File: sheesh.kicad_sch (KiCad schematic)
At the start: 104 parts, among them J1 3305-0-15-80-47-27-10-0, J10 3305-0-15-80-47-27-10-0, J11 3305-0-15-80-47-27-10-0, J12 3305-0-15-80-47-27-10-0, J13 3305-0-15-80-47-27-10-0, J14 3305-0-15-80-47-27-10-0, J15 3305-0-15-80-47-27-10-0, J16 3305-0-15-80-47-27-10-0, J17 3305-0-15-80-47-27-10-0, J18 3305-0-15-80-47-27-10-0, J19 3305-0-15-80-47-27-10-0, J2 3305-0-15-80-47-27-10-0, J20 3305-0-15-80-47-27-10-0, J21 3305-0-15-80-47-27-10-0, J22 3305-0-15-80-47-27-10-0, J23 3305-0-15-80-47-27-10-0, J24 3305-0-15-80-47-27-10-0, J25 3305-0-15-80-47-27-10-0, J26 3305-0-15-80-47-27-10-0, J27 3305-0-15-80-47-27-10-0, J28 3305-0-15-80-47-27-10-0, J29 3305-0-15-80-47-27-10-0, J3 3305-0-15-80-47-27-10-0, J30 3305-0-15-80-47-27-10-0, J31 3305-0-15-80-47-27-10-0, J32 3305-0-15-80-47-27-10-0, J33 3305-0-15-80-47-27-10-0, J34 3305-0-15-80-47-27-10-0, J35 3305-0-15-80-47-27-10-0, J36 3305-0-15-80-47-27-10-0, J37 3305-0-15-80-47-27-10-0, J38 3305-0-15-80-47-27-10-0, J39 3305-0-15-80-47-27-10-0, J4 3305-0-15-80-47-27-10-0, J40 3305-0-15-80-47-27-10-0, J41 3305-0-15-80-47-27-10-0, J42 3305-0-15-80-47-27-10-0, J43 3305-0-15-80-47-27-10-0, J44 3305-0-15-80-47-27-10-0, J45 3305-0-15-80-47-27-10-0, J46 3305-0-15-80-47-27-10-0, J47 3305-0-15-80-47-27-10-0, J48 3305-0-15-80-47-27-10-0, J49 3305-0-15-80-47-27-10-0, J5 3305-0-15-80-47-27-10-0, J50 3305-0-15-80-47-27-10-0, J51 3305-0-15-80-47-27-10-0, J52 3305-0-15-80-47-27-10-0, J53 3305-0-15-80-47-27-10-0, J54 3305-0-15-80-47-27-10-0, J55 3305-0-15-80-47-27-10-0, J56 3305-0-15-80-47-27-10-0, J57 310-13-107-41-001000, J58 310-13-107-41-001000, J59 YZ00615050R-04, J6 3305-0-15-80-47-27-10-0, J60 YZ00615050R-04, J61 YZ00615050R-04, J62 YZ00615050R-04, J63 YZ00615050R-04, J64 310-13-107-41-001000, J65 310-13-107-41-001000, J66 YZ00615050R-04, J67 YZ00615050R-04, J68 YZ00615050R-04, J69 YZ00615050R-04, J7 3305-0-15-80-47-27-10-0, J70 YZ00615050R-04, J8 3305-0-15-80-47-27-10-0, J9 3305-0-15-80-47-27-10-0, SW1 SW_Push, SW10 SW_Push, SW11 SW_Push, SW12 SW_Push, SW13 SW_Push, SW14 SW_Push, SW15 SW_Push, SW16 SW_Push, SW17 SW_Push, SW18 SW_Push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

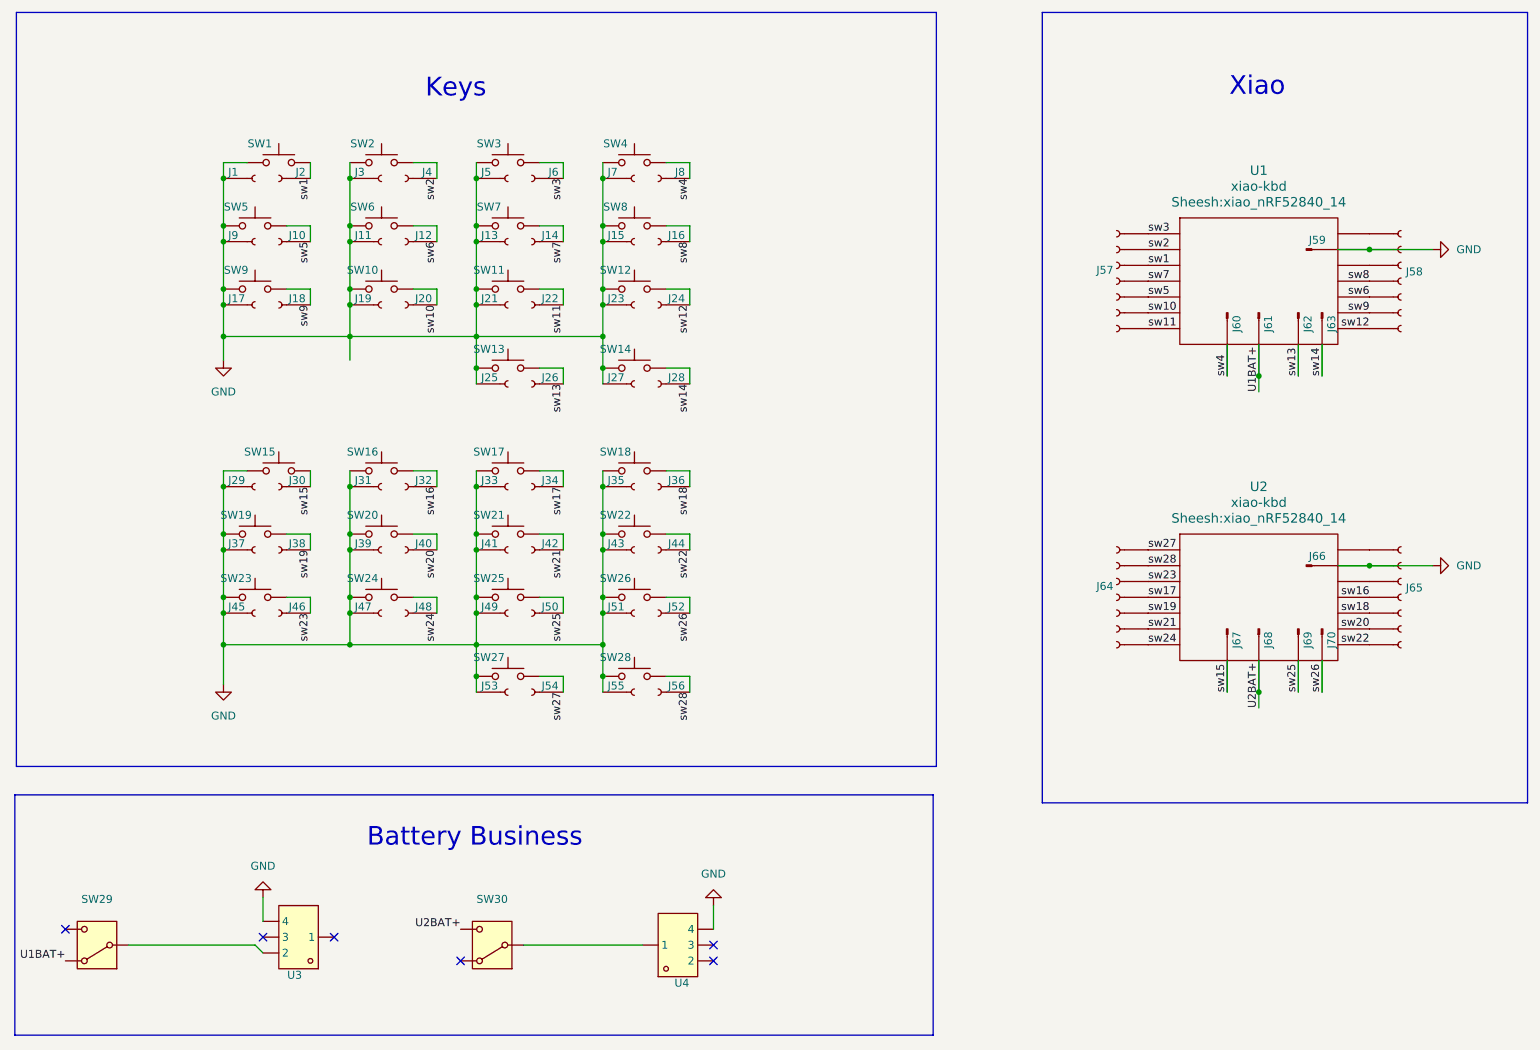
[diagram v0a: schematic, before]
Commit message: fix(sw-th_ssss811101): swap SW29 & SW30 symbol & footprint
Change PCM12SMTR to SSSS811101. The latter fits on the former's footprint, but the location was
slightly off fin  the cpl
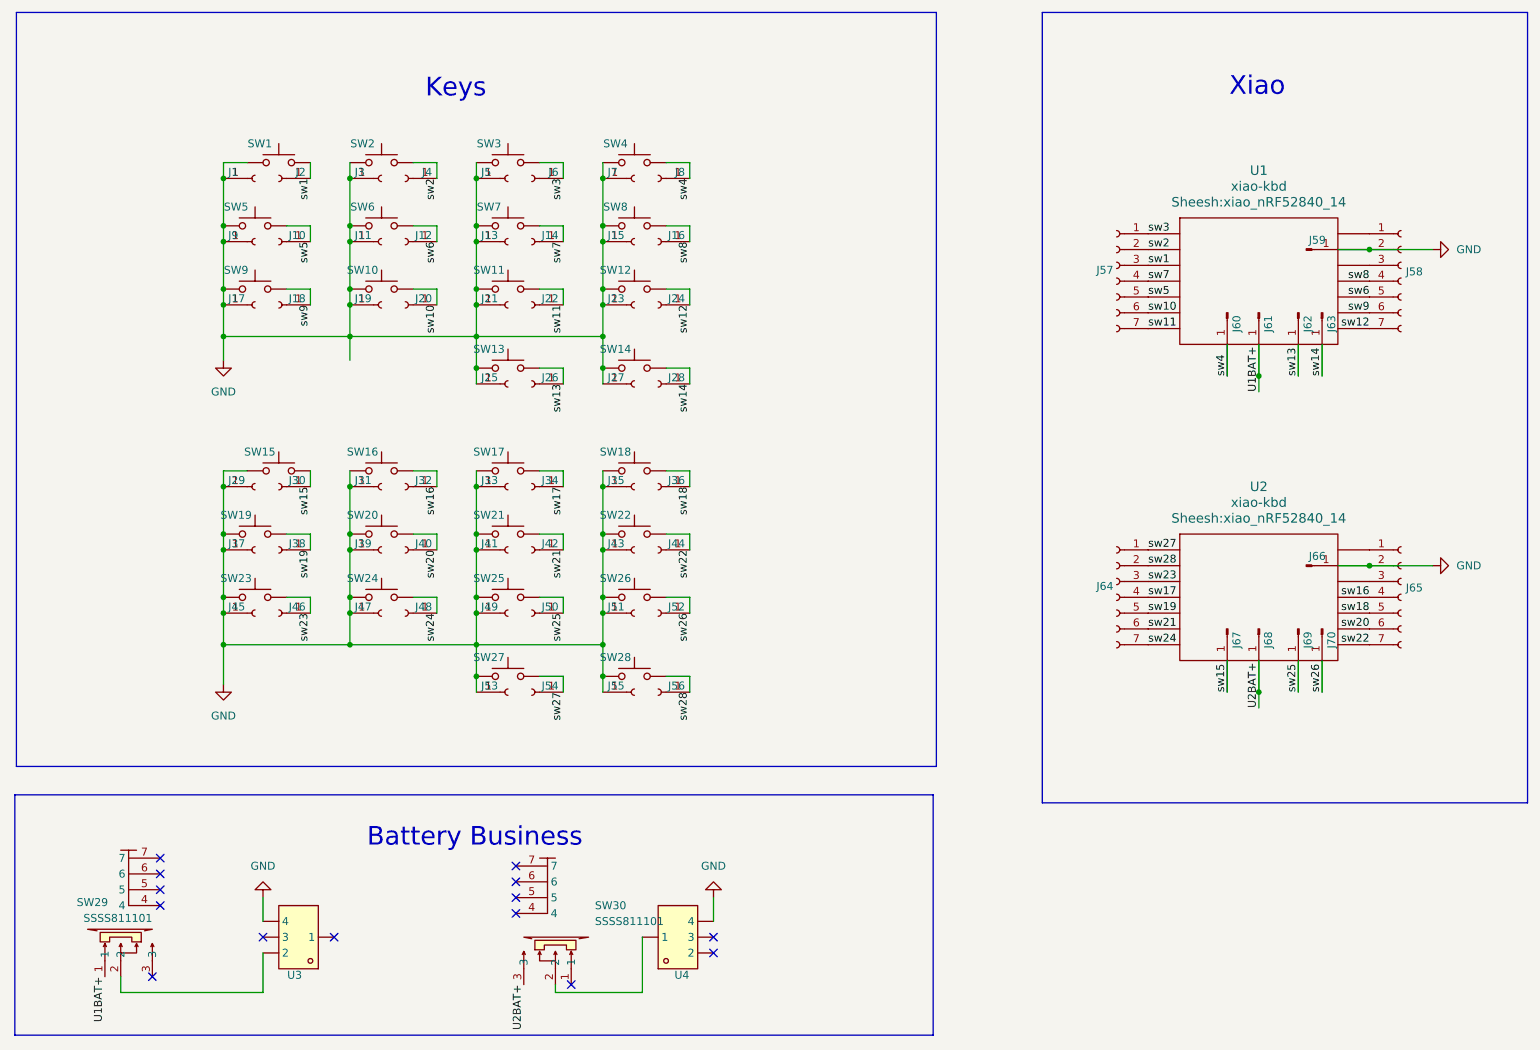
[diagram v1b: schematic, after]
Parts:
- removed SW29, SW30: SSSS811101, Sheesh:SW_PCM12SMTR, symbol Switch:SW_SPDT
- added SW29, SW30: SSSS811101, Sheesh:SW-SMD_SSSS811101, symbol Sheesh:SSSS811101
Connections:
- net U1BAT+: now also SW29.1
- net U2BAT+: now also SW30.3
- net at U4.1: now also SW30.2
- net at U3.2: now also SW29.2
- no-connect marks 6 -> 14
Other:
- moved on the sheet: U4

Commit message: fix(component): correct lcsc field name on ssss811101
correct lcsc field name so it passes kibot filter
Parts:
- SW29, SW30: LCSC (none) -> C109335; LCSC Part C109335 -> (none)
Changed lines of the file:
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@@
 			)
 		)
-		(property "LCSC Part" "C109335"
+		(property "LCSC" "C109335"
 			(at 40.64 151.13 0)
 			(effects
@@
 			)
 		)
-		(property "LCSC Part" "C109335"
+		(property "LCSC" "C109335"
 			(at 113.03 152.4 0)
 			(effects

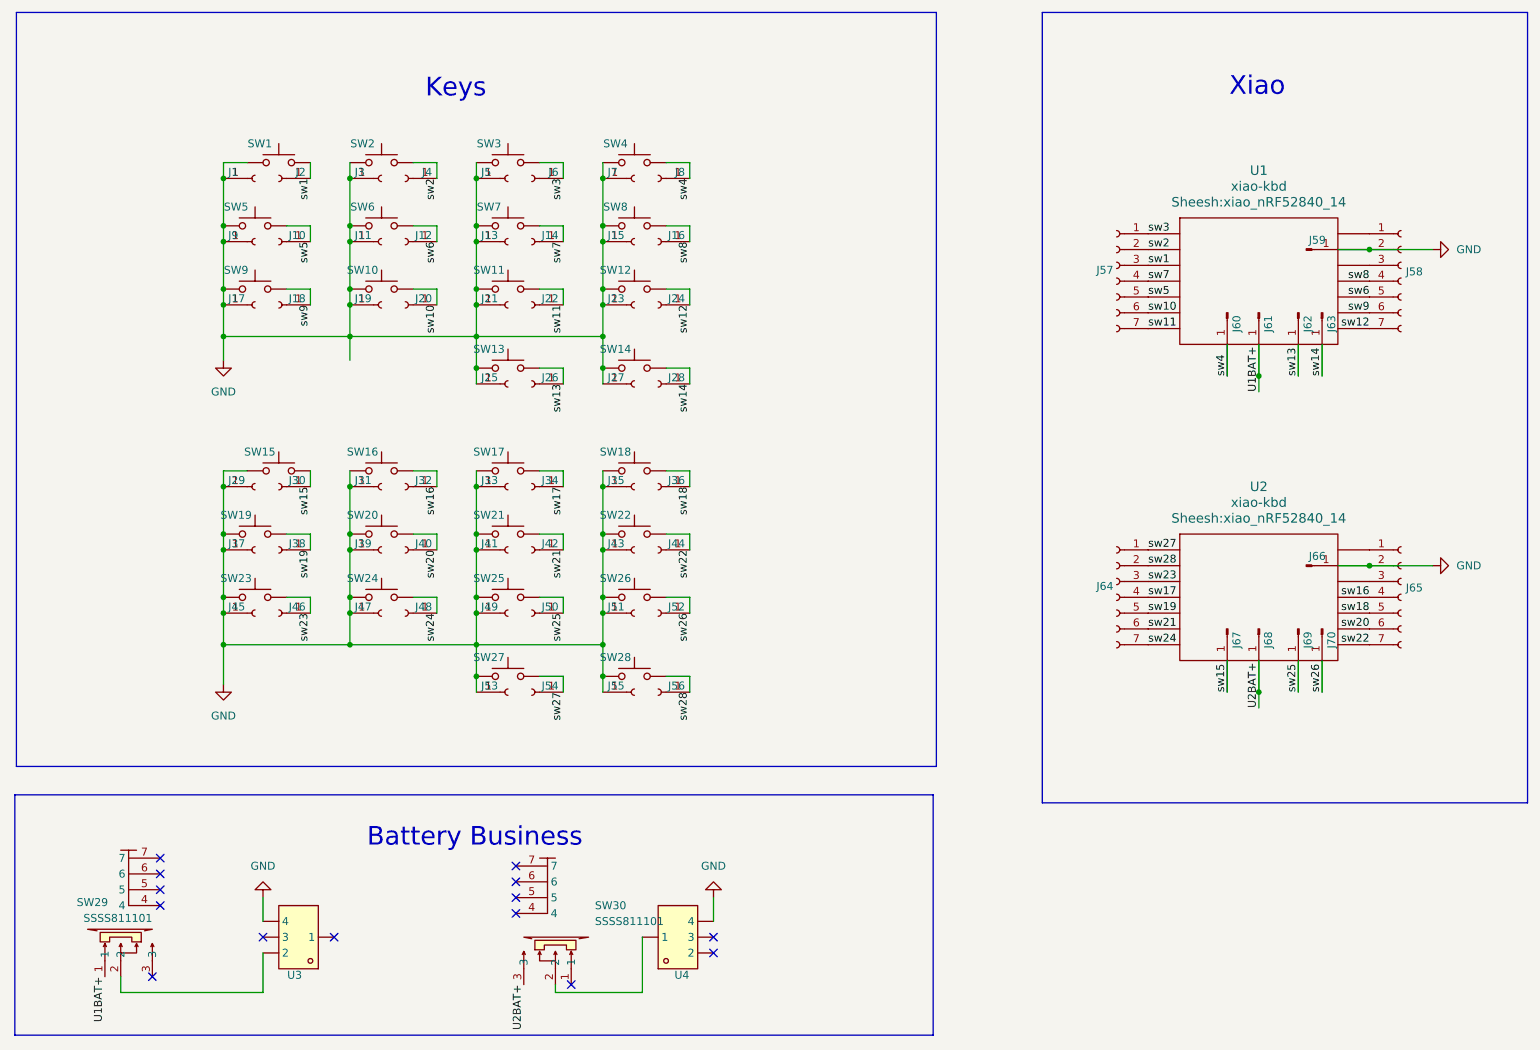
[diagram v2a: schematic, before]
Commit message: switch to diodes
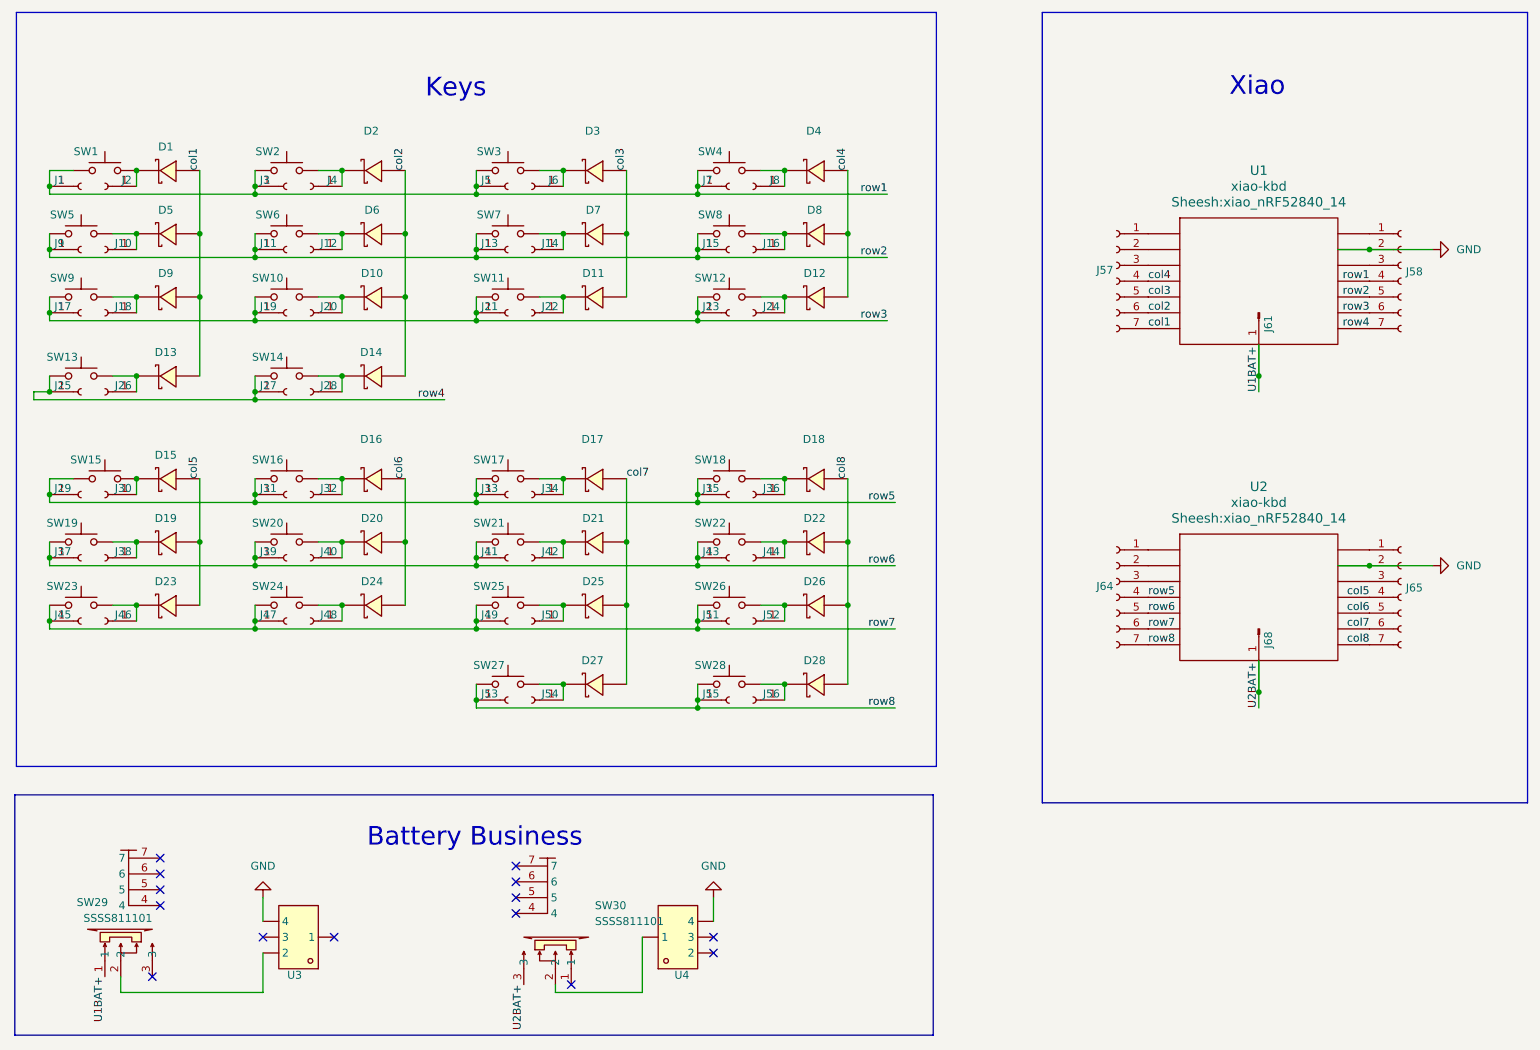
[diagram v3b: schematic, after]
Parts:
- removed J59, J60, J62, J63, J66, J67, J69, J70: YZ00615050R-04, Sheesh:YZ00615050R-04, symbol Connector:Conn_01x01_Pin
- added D1, D10, D11, D12, D13, D14, D15, D16, D17, D18, D19, D2, D20, D21, D22, D23, D24, D25, D26, D27, D28, D3, D4, D5, D6, D7, D8, D9: CDSQC4148-HF, Sheesh:X1-DFN1006-2_L1.0-W0.6-RD, symbol Sheesh:CDSQC4148-HF
- J57, J58, J64, J65: value 310-13-107-41-001000 -> MF254V-11-07-0743
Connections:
- net GND: no longer J1.1 (Pin_1), J11.1 (Pin_1), J13.1 (Pin_1), J15.1 (Pin_1), J17.1 (Pin_1), J19.1 (Pin_1), J21.1 (Pin_1), J23.1 (Pin_1), J25.1 (Pin_1), J27.1 (Pin_1), J29.1 (Pin_1), J3.1 (Pin_1), J31.1 (Pin_1), J33.1 (Pin_1), J35.1 (Pin_1), J37.1 (Pin_1), J39.1 (Pin_1), J41.1 (Pin_1), J43.1 (Pin_1), J45.1 (Pin_1), J47.1 (Pin_1), J49.1 (Pin_1), J5.1 (Pin_1), J51.1 (Pin_1), J53.1 (Pin_1), J55.1 (Pin_1), J7.1 (Pin_1), J9.1 (Pin_1), SW1.1, SW10.1, SW11.1, SW12.1, SW13.1, SW14.1, SW15.1, SW16.1, SW17.1, SW18.1, SW19.1, SW2.1, SW20.1, SW21.1, SW22.1, SW23.1, SW24.1, SW25.1, SW26.1, SW27.1, SW28.1, SW3.1, SW4.1, SW5.1, SW6.1, SW7.1, SW8.1, SW9.1
- net sw1: no longer names the net of J57.3 (Pin_3), U1.3 (D2)
- net sw1: no longer J2.1 (Pin_1), SW1.2
- net sw10: no longer names the net of J20.1 (Pin_1), SW10.2
- net sw10: now also D10.1 (K); no longer J57.6 (Pin_6), U1.6 (D5)
- net sw11: no longer names the net of J22.1 (Pin_1), SW11.2
- net sw11: now also D11.1 (K); no longer J57.7 (Pin_7), U1.7 (D6)
- net sw12: no longer names the net of J24.1 (Pin_1), SW12.2
- net sw12: now also D12.1 (K); no longer J58.7 (Pin_7), U1.8 (D7)
- net sw13: no longer names the net of J26.1 (Pin_1), SW13.2
- net sw13: now also D13.1 (K); no longer U1.15 (NFC1)
- net sw14: no longer names the net of J28.1 (Pin_1), SW14.2
- net sw14: now also D14.1 (K); no longer U1.16 (NFC2)
- net sw15: no longer names the net of J30.1 (Pin_1), SW15.2
- net sw15: now also D15.1 (K); no longer U2.18 (RST)
- net sw16: no longer names the net of J32.1 (Pin_1), SW16.2
- net sw16: now also D16.1 (K); no longer J65.4 (Pin_4), U2.11 (D10)
- net sw17: no longer names the net of J34.1 (Pin_1), SW17.2
- net sw17: now also D17.1 (K); no longer J64.4 (Pin_4), U2.4 (D3)
- net sw18: no longer names the net of J36.1 (Pin_1), SW18.2
- net sw18: now also D18.1 (K); no longer J65.5 (Pin_5), U2.10 (D9)
- net sw19: no longer names the net of J38.1 (Pin_1), SW19.2
- net sw19: now also D19.1 (K); no longer J64.5 (Pin_5), U2.5 (D4)
- net sw2: no longer names the net of J57.2 (Pin_2), U1.2 (D1)
- net sw2: no longer J4.1 (Pin_1), SW2.2
- net sw20: no longer names the net of J40.1 (Pin_1), SW20.2
- net sw20: now also D20.1 (K); no longer J65.6 (Pin_6), U2.9 (D8)
- net sw21: no longer names the net of J42.1 (Pin_1), SW21.2
- net sw21: now also D21.1 (K); no longer J64.6 (Pin_6), U2.6 (D5)
- net sw22: no longer names the net of J44.1 (Pin_1), SW22.2
- net sw22: now also D22.1 (K); no longer J65.7 (Pin_7), U2.8 (D7)
- net sw23: no longer names the net of J64.3 (Pin_3), U2.3 (D2)
- net sw23: no longer J46.1 (Pin_1), SW23.2
- net sw24: no longer names the net of J48.1 (Pin_1), SW24.2
- net sw24: now also D24.1 (K); no longer J64.7 (Pin_7), U2.7 (D6)
- net sw25: no longer names the net of J50.1 (Pin_1), SW25.2
- net sw25: now also D25.1 (K); no longer U2.15 (NFC1)
- net sw26: no longer names the net of J52.1 (Pin_1), SW26.2
- net sw26: now also D26.1 (K); no longer U2.16 (NFC2)
- net sw27: no longer names the net of J64.1 (Pin_1), U2.1 (D0)
- net sw27: no longer J54.1 (Pin_1), SW27.2
- net sw28: no longer names the net of J64.2 (Pin_2), U2.2 (D1)
- net sw28: no longer J56.1 (Pin_1), SW28.2
- net sw3: no longer names the net of J6.1 (Pin_1), SW3.2
- net sw3: now also D3.1 (K); no longer J57.1 (Pin_1), U1.1 (D0)
- net sw4: no longer names the net of J8.1 (Pin_1), SW4.2
- net sw4: now also D4.1 (K); no longer U1.18 (RST)
- net sw5: no longer names the net of J10.1 (Pin_1), SW5.2
- net sw5: now also D5.1 (K); no longer J57.5 (Pin_5), U1.5 (D4)
- net sw6: no longer names the net of J12.1 (Pin_1), SW6.2
- net sw6: now also D6.1 (K); no longer J58.5 (Pin_5), U1.10 (D9)
- net sw7: no longer names the net of J14.1 (Pin_1), SW7.2
- net sw7: now also D7.1 (K); no longer J57.4 (Pin_4), U1.4 (D3)
- net sw8: no longer names the net of J16.1 (Pin_1), SW8.2
- net sw8: now also D8.1 (K); no longer J58.4 (Pin_4), U1.11 (D10)
- net sw9: no longer names the net of J18.1 (Pin_1), SW9.2
- net sw9: now also D9.1 (K); no longer J58.6 (Pin_6), U1.9 (D8)
- new net: J57.1 (Pin_1), U1.1 (D0)
- new net: D28.1 (K), J56.1 (Pin_1), SW28.2
- new net: D27.1 (K), J54.1 (Pin_1), SW27.2
- new net: D23.1 (K), J46.1 (Pin_1), SW23.2
- new net: D2.1 (K), J4.1 (Pin_1), SW2.2
- new net: D1.1 (K), J2.1 (Pin_1), SW1.2
- new net col1: D1.2 (A), D13.2 (A), D5.2 (A), D9.2 (A), J57.7 (Pin_7), U1.7 (D6)
- new net col2: D10.2 (A), D14.2 (A), D2.2 (A), D6.2 (A), J57.6 (Pin_6), U1.6 (D5)
- new net col3: D11.2 (A), D3.2 (A), D7.2 (A), J57.5 (Pin_5), U1.5 (D4)
- new net col4: D12.2 (A), D4.2 (A), D8.2 (A), J57.4 (Pin_4), U1.4 (D3)
- new net col5: D15.2 (A), D19.2 (A), D23.2 (A), J65.4 (Pin_4), U2.11 (D10)
- new net col6: D16.2 (A), D20.2 (A), D24.2 (A), J65.5 (Pin_5), U2.10 (D9)
- new net col7: D17.2 (A), D21.2 (A), D25.2 (A), D27.2 (A), J65.6 (Pin_6), U2.9 (D8)
- new net col8: D18.2 (A), D22.2 (A), D26.2 (A), D28.2 (A), J65.7 (Pin_7), U2.8 (D7)
- new net row1: J1.1 (Pin_1), J3.1 (Pin_1), J5.1 (Pin_1), J58.4 (Pin_4), J7.1 (Pin_1), SW1.1, SW2.1, SW3.1, SW4.1, U1.11 (D10)
- new net row2: J11.1 (Pin_1), J13.1 (Pin_1), J15.1 (Pin_1), J58.5 (Pin_5), J9.1 (Pin_1), SW5.1, SW6.1, SW7.1, SW8.1, U1.10 (D9)
- new net row3: J17.1 (Pin_1), J19.1 (Pin_1), J21.1 (Pin_1), J23.1 (Pin_1), J58.6 (Pin_6), SW10.1, SW11.1, SW12.1, SW9.1, U1.9 (D8)
- new net row4: J25.1 (Pin_1), J27.1 (Pin_1), J58.7 (Pin_7), SW13.1, SW14.1, U1.8 (D7)
- new net row5: J29.1 (Pin_1), J31.1 (Pin_1), J33.1 (Pin_1), J35.1 (Pin_1), J64.4 (Pin_4), SW15.1, SW16.1, SW17.1, SW18.1, U2.4 (D3)
- new net row6: J37.1 (Pin_1), J39.1 (Pin_1), J41.1 (Pin_1), J43.1 (Pin_1), J64.5 (Pin_5), SW19.1, SW20.1, SW21.1, SW22.1, U2.5 (D4)
- new net row7: J45.1 (Pin_1), J47.1 (Pin_1), J49.1 (Pin_1), J51.1 (Pin_1), J64.6 (Pin_6), SW23.1, SW24.1, SW25.1, SW26.1, U2.6 (D5)
- new net row8: J53.1 (Pin_1), J55.1 (Pin_1), J64.7 (Pin_7), SW27.1, SW28.1, U2.7 (D6)
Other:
- moved on the sheet: J1, J10, J11, J12, J13, J14, J15, J16, J17, J18, J19, J2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
